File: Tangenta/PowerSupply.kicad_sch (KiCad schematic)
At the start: 57 parts, among them J1 39281243, U1 TPS54331DR, U2 TPS54331DR, U3 TPS54331DR, U4 TPS54331DR

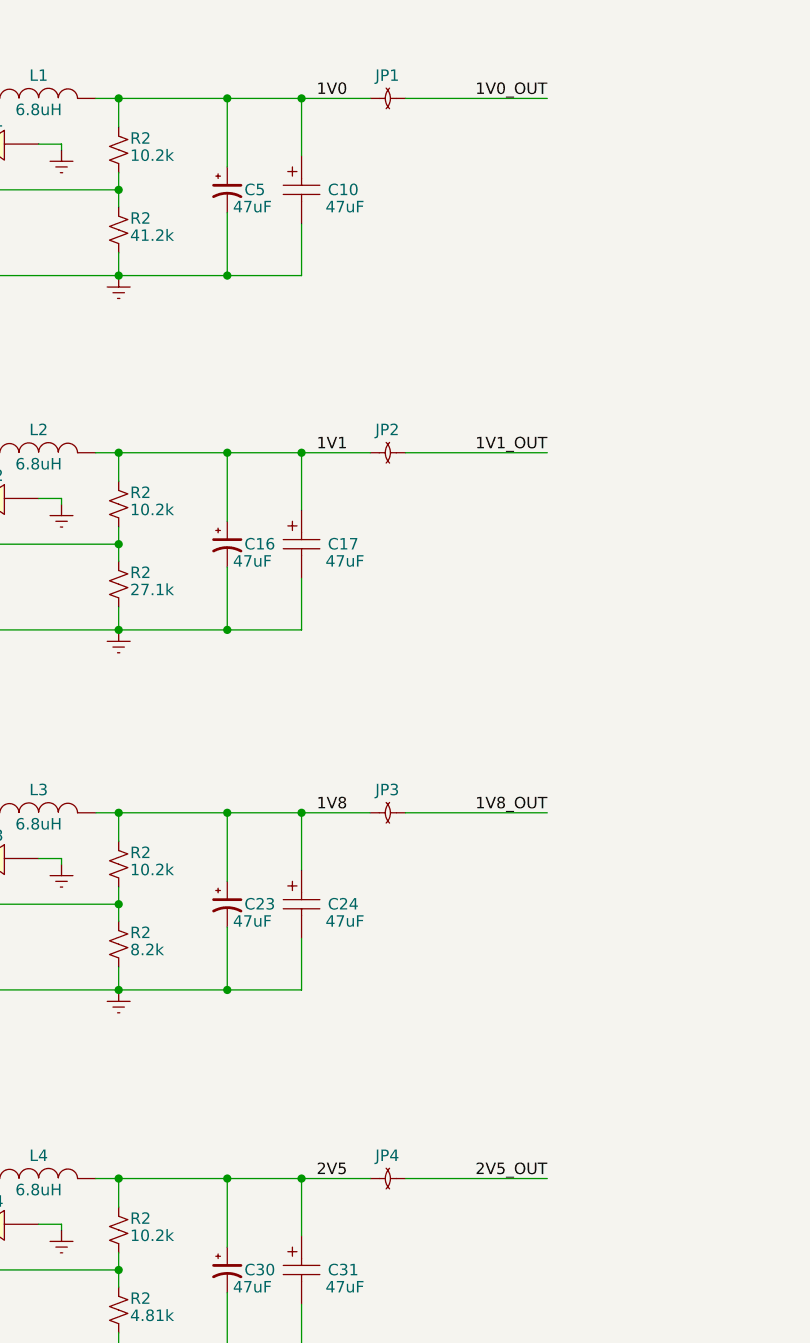
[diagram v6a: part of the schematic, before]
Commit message: USB dual role routed.
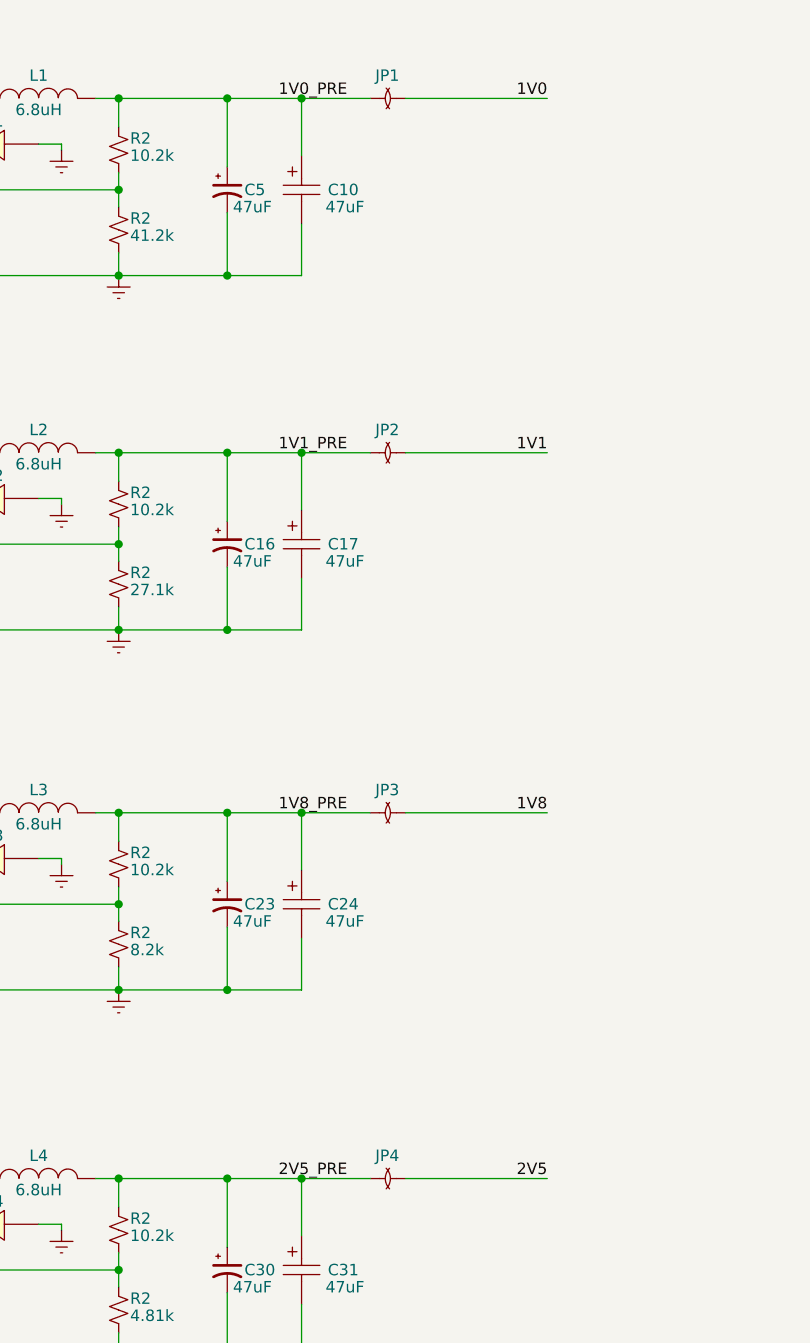
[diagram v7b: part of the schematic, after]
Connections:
- net 1V0_OUT is gone; now on net 1V0: JP1.2
- net 1V1_OUT is gone; now on net 1V1: JP2.2
- net 1V8_OUT is gone; now on net 1V8: JP3.2
- net 2V5_OUT is gone; now on net 2V5: JP4.2
- net 1V0: no longer C10.1, C5.1, JP1.1, L1.1, R2.1
- net 1V1: no longer C16.1, C17.1, JP2.1, L2.1, R2.1
- net 1V8: no longer C23.1, C24.1, JP3.1, L3.1, R2.1
- net 2V5: no longer C30.1, C31.1, JP4.1, L4.1, R2.1
- new net 1V0_PRE: C10.1, C5.1, JP1.1, L1.1, R2.1
- new net 1V1_PRE: C16.1, C17.1, JP2.1, L2.1, R2.1
- new net 1V8_PRE: C23.1, C24.1, JP3.1, L3.1, R2.1
- new net 2V5_PRE: C30.1, C31.1, JP4.1, L4.1, R2.1
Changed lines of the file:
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@@
     (effects (font (size 1.27 1.27)) (justify right bottom))
   )
-  (label "1V0" (at 156.845 24.13 180) (fields_autoplaced)
+  (label "1V0_PRE" (at 156.845 24.13 180) (fields_autoplaced)
     (effects (font (size 1.27 1.27)) (justify right bottom))
   )
-  (label "2V5_OUT" (at 179.07 144.145 180) (fields_autoplaced)
+  (label "2V5" (at 179.07 144.145 180) (fields_autoplaced)
     (effects (font (size 1.27 1.27)) (justify right bottom))
   )
@@
     (effects (font (size 1.27 1.27)) (justify right bottom))
   )
-  (label "1V8_OUT" (at 179.07 103.505 180) (fields_autoplaced)
+  (label "1V8" (at 179.07 103.505 180) (fields_autoplaced)
     (effects (font (size 1.27 1.27)) (justify right bottom))
   )
-  (label "1V8" (at 156.845 103.505 180) (fields_autoplaced)
+  (label "1V8_PRE" (at 156.845 103.505 180) (fields_autoplaced)
     (effects (font (size 1.27 1.27)) (justify right bottom))
   )
@@
     (effects (font (size 1.27 1.27)) (justify left bottom))
   )
-  (label "1V0_OUT" (at 179.07 24.13 180) (fields_autoplaced)
+  (label "1V0" (at 179.07 24.13 180) (fields_autoplaced)
     (effects (font (size 1.27 1.27)) (justify right bottom))
   )
@@
     (effects (font (size 1.27 1.27)) (justify left bottom))
   )
-  (label "2V5" (at 156.845 144.145 180) (fields_autoplaced)
+  (label "2V5_PRE" (at 156.845 144.145 180) (fields_autoplaced)
     (effects (font (size 1.27 1.27)) (justify right bottom))
   )
@@
     (effects (font (size 1.27 1.27)) (justify left bottom))
   )
-  (label "1V1" (at 156.845 63.5 180) (fields_autoplaced)
+  (label "1V1_PRE" (at 156.845 63.5 180) (fields_autoplaced)
     (effects (font (size 1.27 1.27)) (justify right bottom))
   )
@@
     (effects (font (size 1.27 1.27)) (justify right bottom))
   )
-  (label "1V1_OUT" (at 179.07 63.5 180) (fields_autoplaced)
+  (label "1V1" (at 179.07 63.5 180) (fields_autoplaced)
     (effects (font (size 1.27 1.27)) (justify right bottom))
   )

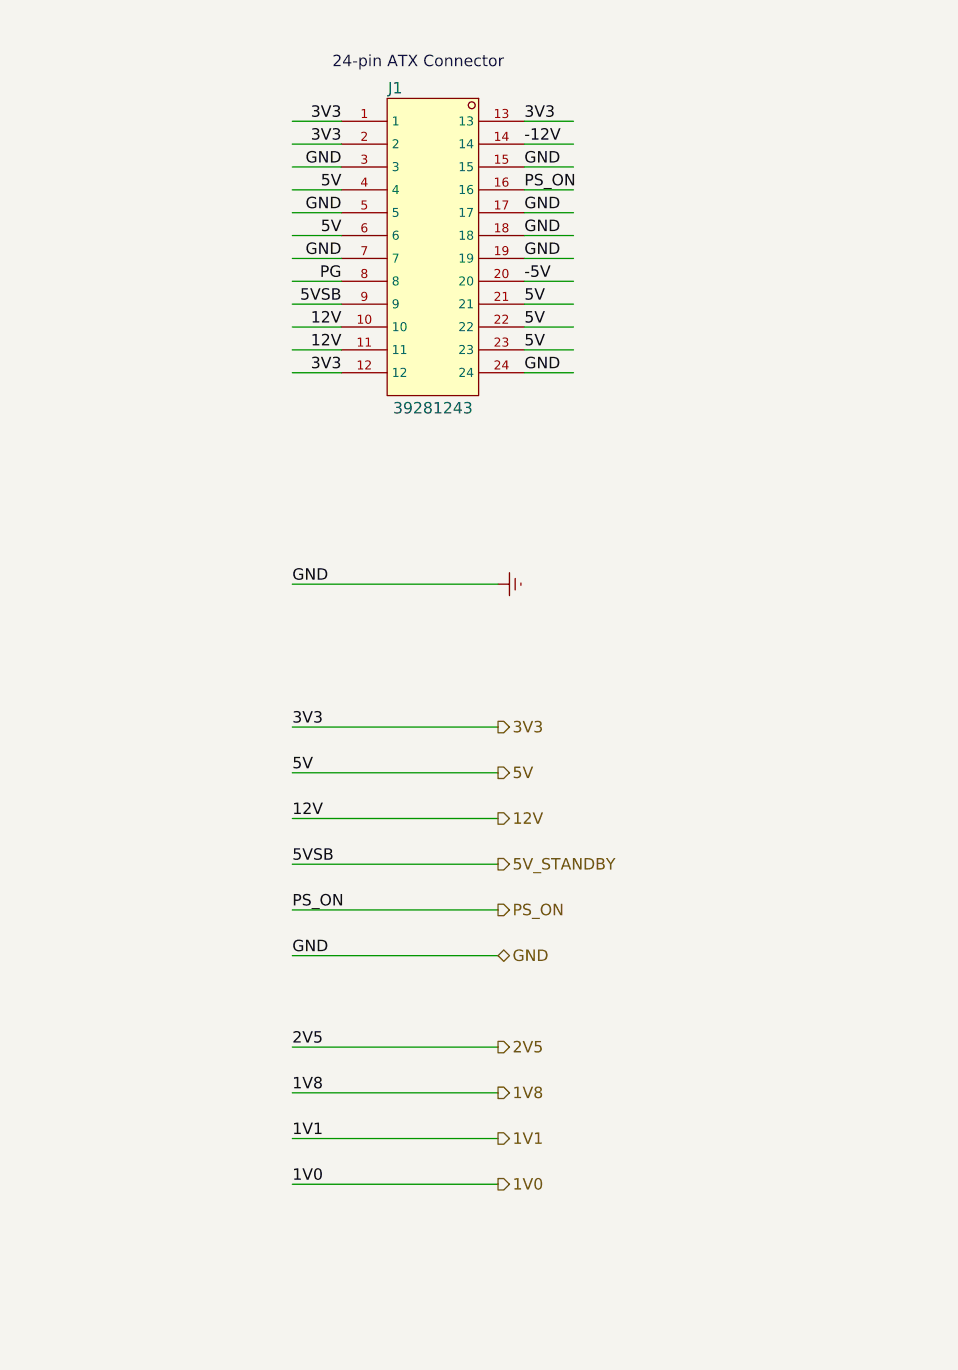
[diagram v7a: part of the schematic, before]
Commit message: Adding 3V3 standby for the PCIe
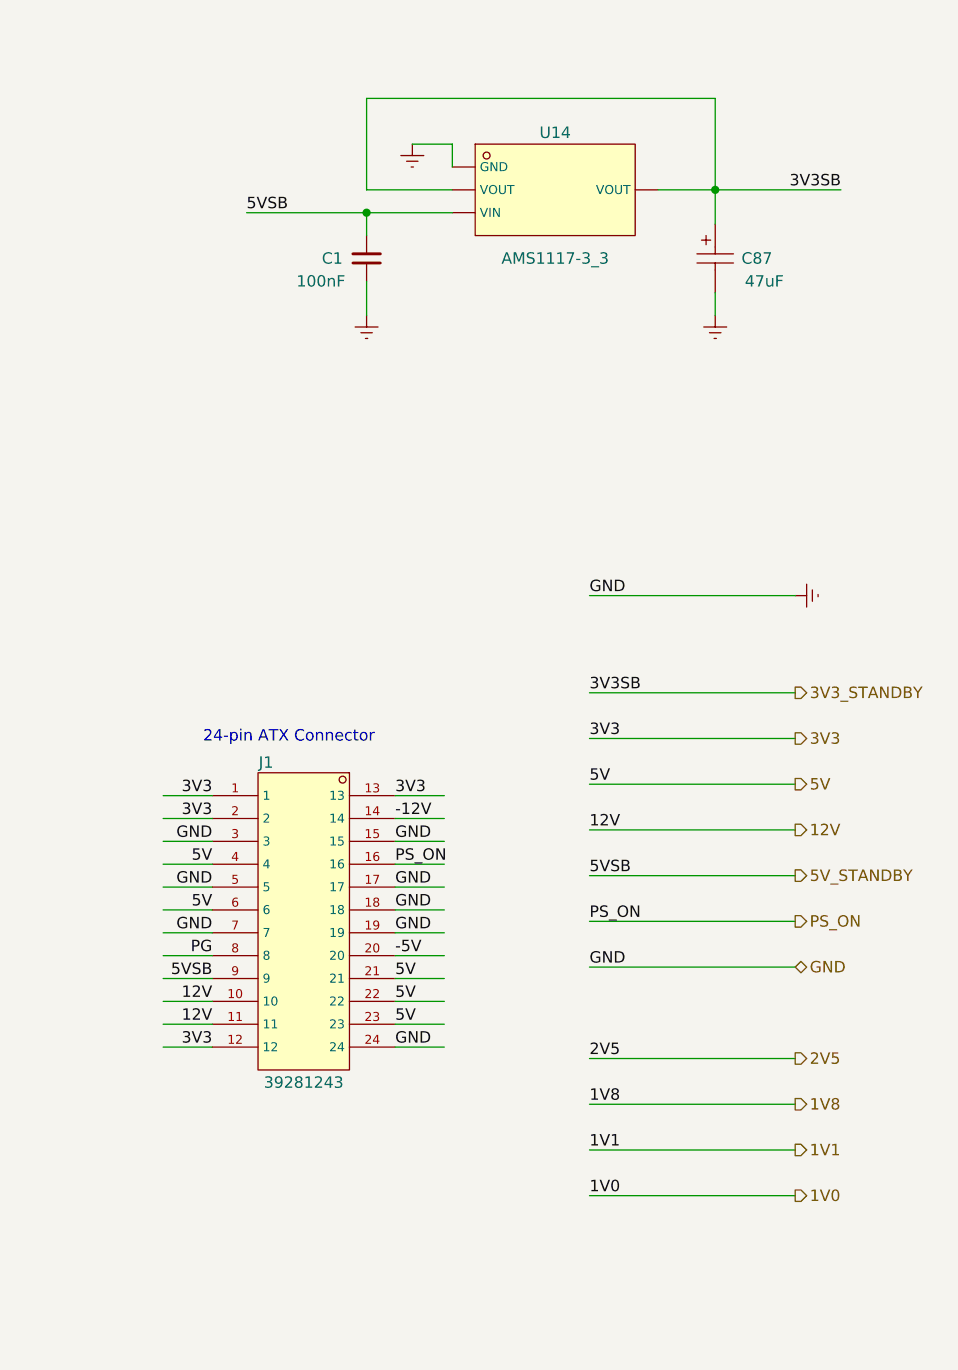
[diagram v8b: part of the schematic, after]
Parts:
- added C1: 100nF, Capacitor_SMD:C_0603_1608Metric, symbol Device:C_Small
- added C87: 47uF, CAP_TANTAL_A:CAP_TANTAL_A, symbol CAP_TANTAL_A:CA45-A-6_3V-47UF-K
- added U14: AMS1117-3_3, AMS1117-3.3:AMS1117-3.3, symbol AMS1117-3.3:AMS1117-3_3
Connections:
- net 5V_STANDBY: now also C1.2, U14.3 (VIN)
- net GNDREF: now also C1.1, C87.2, U14.1 (GND)
- new net 3V3_STANDBY: C87.1, U14.2 (VOUT), U14.4 (VOUT)
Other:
- moved on the sheet: J1
